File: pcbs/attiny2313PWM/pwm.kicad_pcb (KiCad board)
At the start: 2 copper layers, 147 x 87.1 mm, 37 parts, among them IC1 ATTINY2313A-P, Q1 IRF540N, Q2 IRF540N, Q3 IRF540N, Q4 IRF540N, U1 SP3485CP, Y1 Crystal

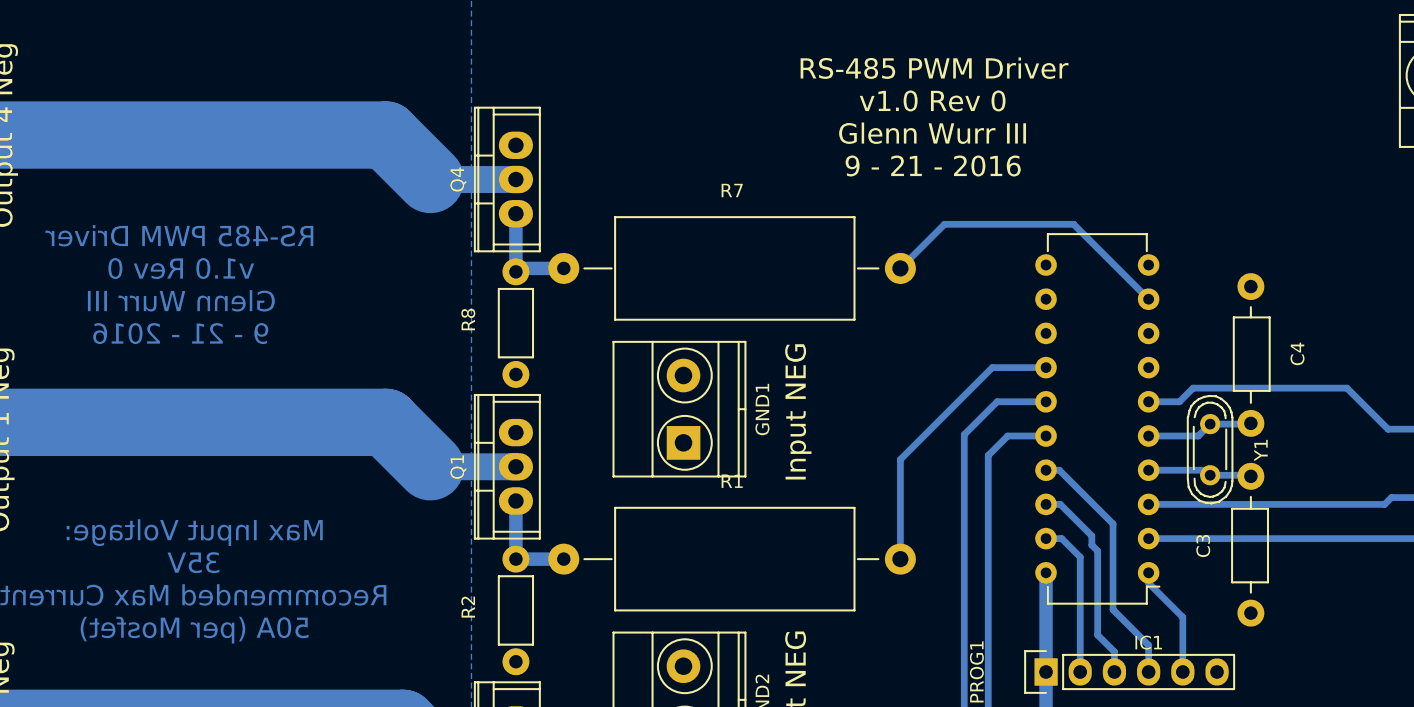
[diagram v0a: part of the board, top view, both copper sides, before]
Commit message: fixed footprint on crystal
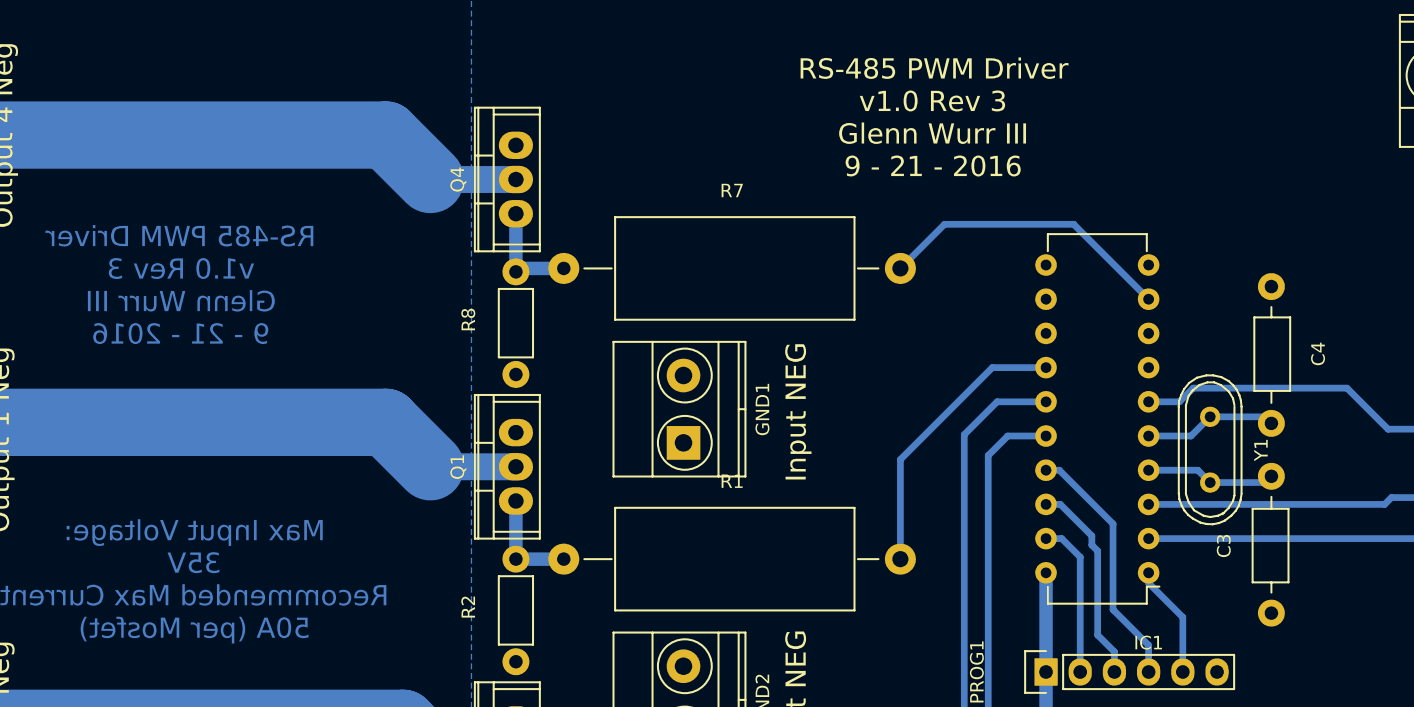
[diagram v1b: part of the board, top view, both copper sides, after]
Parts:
- Y1: footprint Crystals:Crystal_HC52-U_Vertical -> Crystals:Crystal_HC49-U_Vertical
- moved C3 1.52 mm to (183.9, 105.8)
- moved C4 1.52 mm to (183.9, 91.6)
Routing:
- net Net-(C3-Pad2): track 7.97 -> 10.2 mm
- net Net-(C4-Pad2): track 8.17 -> 10.1 mm
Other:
- board text added: "RS-485 PWM Driver v1.0 Rev 3 Glenn Wurr III 9 - 21 - 2016"
- board text removed: "RS-485 PWM Driver v1.0 Rev 0 Glenn Wurr III 9 - 21 - 2016"
